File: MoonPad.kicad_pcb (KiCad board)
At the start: 4 copper layers, 44.5 x 40.6 mm, 61 parts, among them IC1 W25Q16JVUXIQ, J1 OLED, J3 USB-C 2.0 Receptacle, SW1 Reset, U3 RP2040, U4 SLSS49E-3, U5 SLSS49E-3, U6 AP2112K-3.3, Y1 JGHC S3212000181080

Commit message: Fixed libraries
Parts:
- D4: footprint kicad-keyboard-parts:MX_SK6812MINI-E_REV -> Moonpad:MX_SK6812MINI-E_REV
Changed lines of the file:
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@@
     )
   )
-  (footprint "kicad-keyboard-parts:MX_SK6812MINI-E_REV" (layer "F.Cu")
+  (footprint "Moonpad:MX_SK6812MINI-E_REV" (layer "F.Cu")
     (at 156.21 110.49)
     (descr "Add-on for regular MX-footprints with SK6812 MINI-E")
@@
     (fp_arc (start 1.046711 -1.592299) (mid 1.638072 -1.528035) (end 1.749484 -0.943719)
       (stroke (width 0.1) (type solid)) (layer "Edge.Cuts"))
-    (fp_arc (start 1.699999 -0.726842) (mid 1.712528 -0.838068) (end 1.749484 -0.94372)
+    (fp_arc (start 1.699999 -0.726842) (mid 1.712527 -0.838068) (end 1.749484 -0.94372)
       (stroke (width 0.1) (type solid)) (layer "Edge.Cuts"))
     (fp_arc (start 1.749484 0.89572) (mid 1.63807 1.480034) (end 1.046711 1.544298)
@@
       (rotate (xyz 0 0 0))
     )
-    (model "${KIPRJMOD}/Libraries/kicad-keyboard-parts.pretty/3d/LED_SK6812MINI-E.step"
+    (model "${KIPRJMOD}/Libraries/marbastlib/3dmodels/LED_SK6812MINI-E.step"
       (offset (xyz 0 -5.08 -1.778))
       (scale (xyz 1 1 1))
@@
     (fp_arc (start 1.046711 -1.592299) (mid 1.638072 -1.528035) (end 1.749484 -0.943719)
       (stroke (width 0.1) (type solid)) (layer "Edge.Cuts"))
-    (fp_arc (start 1.699999 -0.726842) (mid 1.712528 -0.838068) (end 1.749484 -0.94372)
+    (fp_arc (start 1.699999 -0.726842) (mid 1.712527 -0.838068) (end 1.749484 -0.94372)
       (stroke (width 0.1) (type solid)) (layer "Edge.Cuts"))
     (fp_arc (start 1.749484 0.89572) (mid 1.63807 1.480034) (end 1.046711 1.544298)
@@
       (rotate (xyz 0 0 0))
     )
-    (model "${KIPRJMOD}/Libraries/kicad-keyboard-parts.pretty/3d/LED_SK6812MINI-E.step"
+    (model "${KIPRJMOD}/Libraries/marbastlib/3dmodels/LED_SK6812MINI-E.step"
       (offset (xyz 0 -5.08 -1.778))
       (scale (xyz 1 1 1))

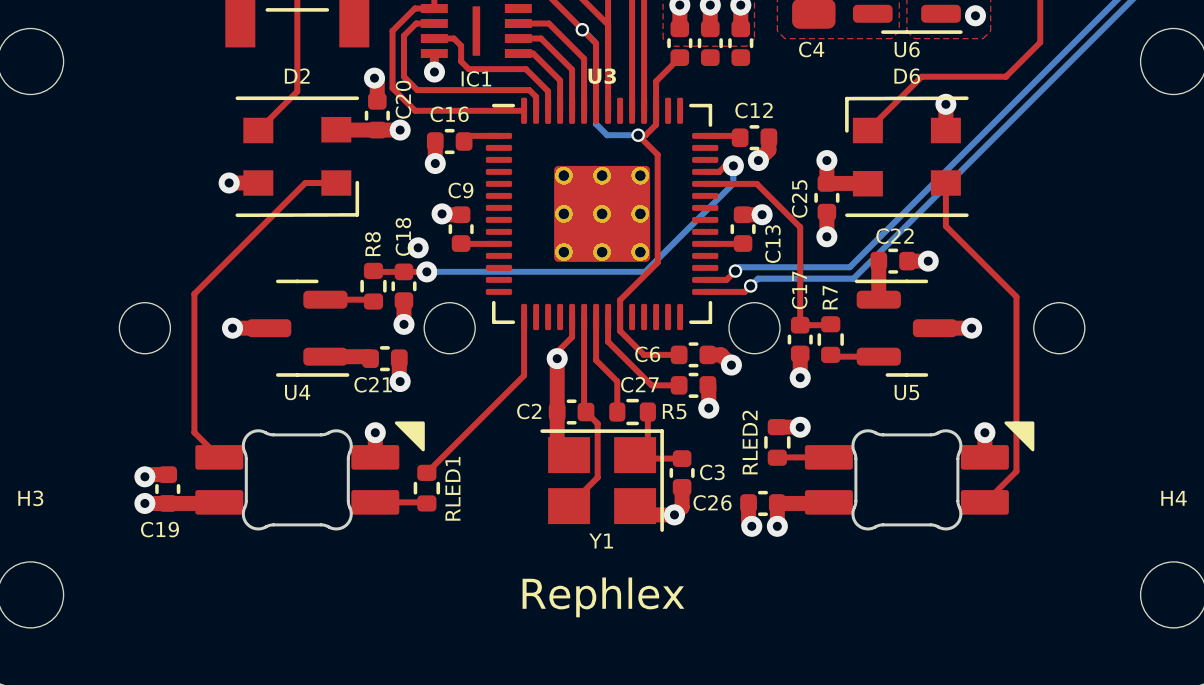
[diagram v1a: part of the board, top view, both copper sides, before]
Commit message: Edited some 3d. Now sent for manufacturing.
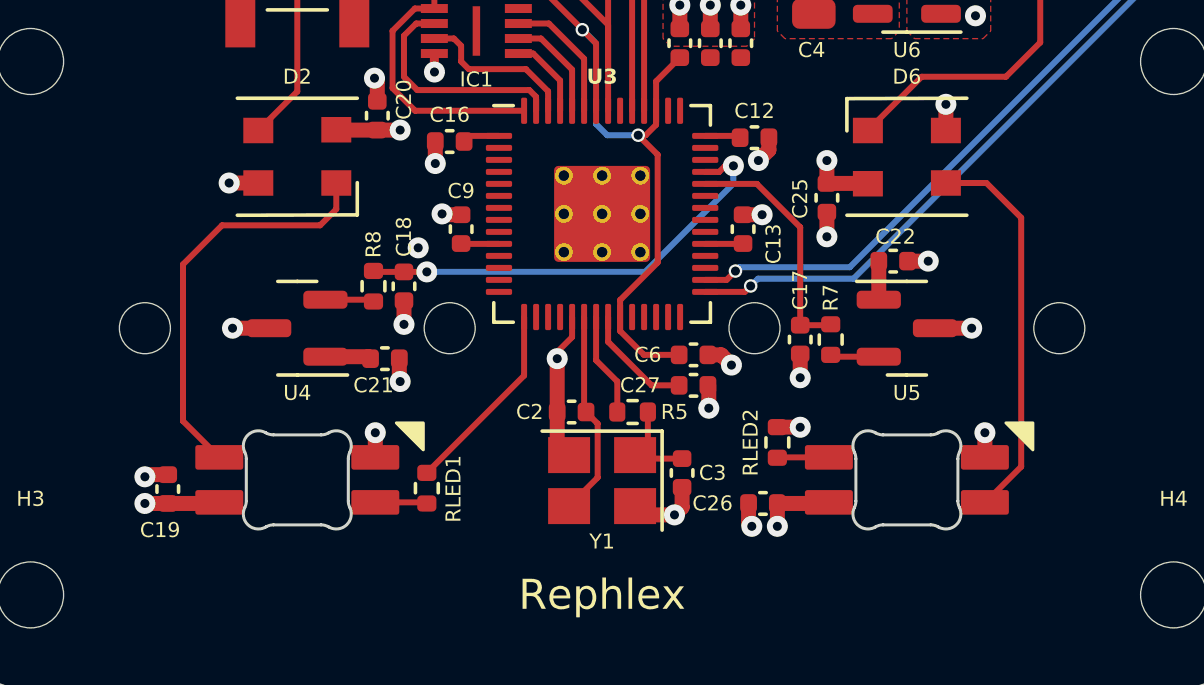
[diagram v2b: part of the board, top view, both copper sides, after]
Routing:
- net Net-(D1-DOUT): track 12.1 -> 13.7 mm
- net Net-(D4-DIN): track 12.1 -> 13.0 mm
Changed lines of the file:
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@@
       (net 2 "GND") (pinfunction "SHIELD") (pintype "passive"))
     (model "${KIPRJMOD}/Libraries/TYPE-C-31-M-12--3DModel-STEP-56544.STEP"
-      (offset (xyz 0 -1.143 0))
+      (offset (xyz 0 -1.05 0))
       (scale (xyz 1 1 1))
       (rotate (xyz 90 180 180))
@@
     (property "ki_description" "Resistor")
     (property "ki_keywords" "R res resistor")
-    (attr smd)
+    (attr smd exclude_from_pos_files exclude_from_bom)
     (fp_text reference "R9" (at 0 1.257236) (layer "F.SilkS") hide
         (effects (font (size 0.5 0.5) (thickness 0.125)))
@@
       (rotate (xyz 0 0 0))
     )
+    (model "${KIPRJMOD}/shapes3D/OLED-Module-with-Pins.wrl"
+      (offset (xyz 0 -3.81 0))
+      (scale (xyz 1 1 1))
+      (rotate (xyz 0 0 -90))
+    )
   )
   (gr_rect (start 125.73 95.25) (end 166.37 115.57)
@@
   (segment (start 135.89 97.52) (end 134.59 98.82) (width 0.2) (layer "F.Cu") (net 60))
   (segment (start 137.19 85.33) (end 135.89 86.63) (width 0.2) (layer "F.Cu") (net 60))
-  (segment (start 132.461 104.267) (end 132.461 108.887) (width 0.2) (layer "F.Cu") (net 61))
-  (segment (start 137.19 100.57) (end 136.158 100.57) (width 0.2) (layer "F.Cu") (net 61))
-  (segment (start 136.158 100.57) (end 132.461 104.267) (width 0.2) (layer "F.Cu") (net 61))
-  (segment (start 132.461 108.887) (end 133.29 109.716) (width 0.2) (layer "F.Cu") (net 61))
+  (segment (start 137.19 100.57) (end 137.19 101.443) (width 0.2) (layer "F.Cu") (net 61))
+  (segment (start 132.08 103.28275) (end 132.08 108.506) (width 0.2) (layer "F.Cu") (net 61))
+  (segment (start 137.19 101.443) (end 136.652 101.981) (width 0.2) (layer "F.Cu") (net 61))
+  (segment (start 133.38175 101.981) (end 132.08 103.28275) (width 0.2) (layer "F.Cu") (net 61))
+  (segment (start 132.08 108.506) (end 133.29 109.716) (width 0.2) (layer "F.Cu") (net 61))
+  (segment (start 136.652 101.981) (end 133.38175 101.981) (width 0.2) (layer "F.Cu") (net 61))
   (segment (start 138.49 111.216) (end 140.172 111.216) (width 0.2) (layer "F.Cu") (net 62))
   (segment (start 140.172 111.216) (end 140.208 111.252) (width 0.2) (layer "F.Cu") (net 62))
@@
   (segment (start 160.655 87.503) (end 158.482 85.33) (width 0.2) (layer "F.Cu") (net 63))
   (segment (start 160.655 95.885) (end 160.655 87.503) (width 0.2) (layer "F.Cu") (net 63))
-  (segment (start 157.51 102.011) (end 159.8624 104.3634) (width 0.2) (layer "F.Cu") (net 64))
-  (segment (start 159.8624 104.3634) (end 159.8624 110.182513) (width 0.2) (layer "F.Cu") (net 64))
-  (segment (start 159.8624 110.182513) (end 158.828913 111.216) (width 0.2) (layer "F.Cu") (net 64))
+  (segment (start 160.02 110.024913) (end 158.828913 111.216) (width 0.2) (layer "F.Cu") (net 64))
+  (segment (start 160.02 101.727) (end 160.02 110.024913) (width 0.2) (layer "F.Cu") (net 64))
   (segment (start 158.828913 111.216) (end 158.81 111.216) (width 0.2) (layer "F.Cu") (net 64))
-  (segment (start 157.51 100.57) (end 157.51 102.011) (width 0.2) (layer "F.Cu") (net 64))
+  (segment (start 157.51 100.57) (end 158.863 100.57) (width 0.2) (layer "F.Cu") (net 64))
+  (segment (start 158.863 100.57) (end 160.02 101.727) (width 0.2) (layer "F.Cu") (net 64))
   (segment (start 131.572 111.252) (end 133.254 111.252) (width 0.5) (layer "F.Cu") (net 65))
   (segment (start 138.557 83.566) (end 139.319 83.566) (width 0.5) (layer "F.Cu") (net 65))

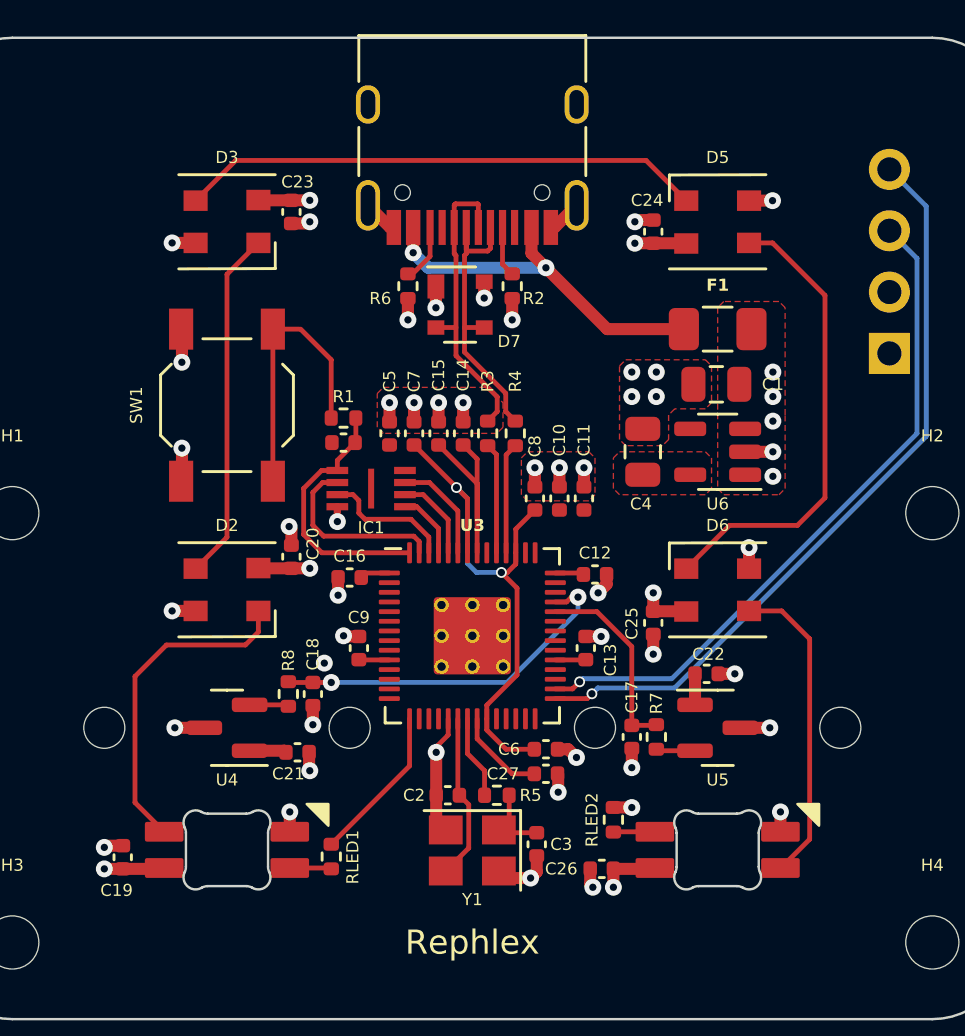
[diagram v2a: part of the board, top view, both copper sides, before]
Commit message: Cost optimisation + case files
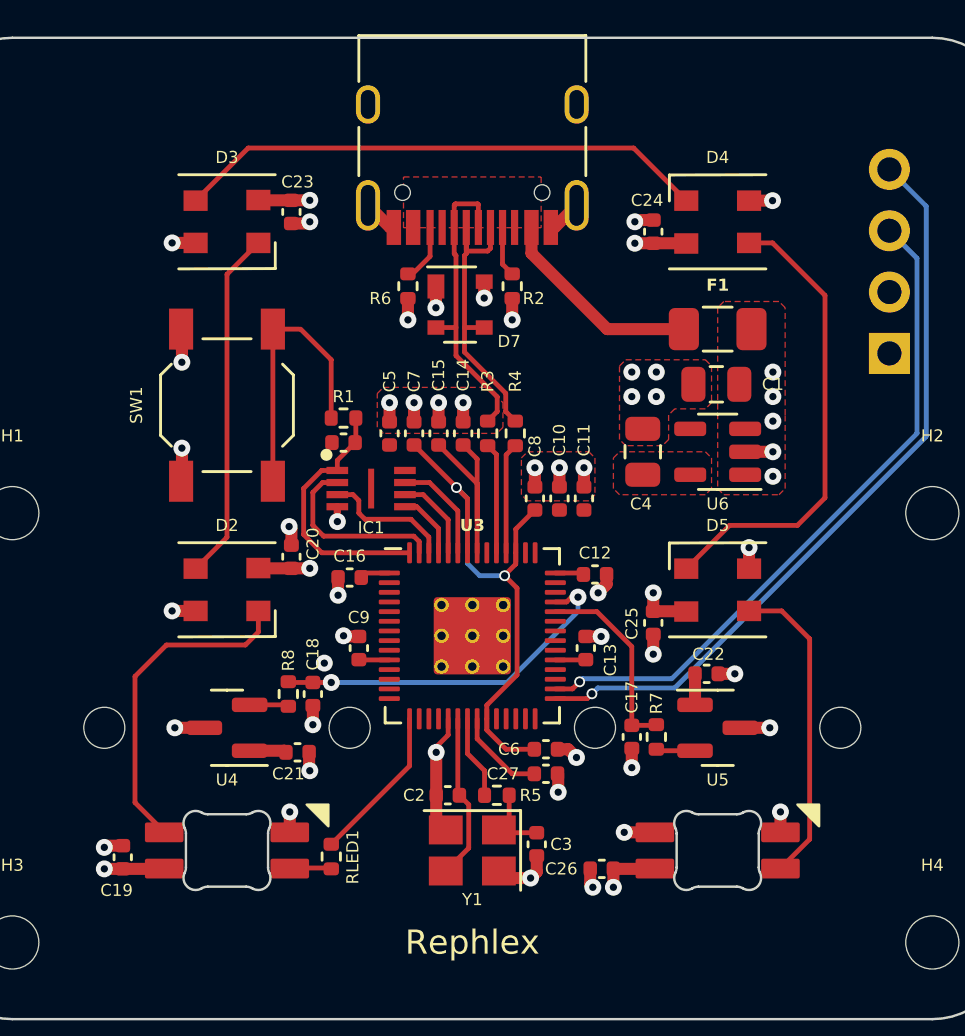
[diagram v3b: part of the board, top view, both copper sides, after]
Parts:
- removed RLED2: 470, Resistor_SMD:R_0402_1005Metric
- C2, C3: value 27p -> 30p
- D6: renamed from D4; footprint Moonpad:MX_SK6812MINI-E_REV -> kicad-keyboard-parts:MX_SK6812MINI-E_REV
- Y1: value JGHC S3212000181080 -> X322512MSB4SI
- moved D1 0.10 mm to (135.8, 110.5)
- moved D6 0.10 mm to (156.1, 110.5)
- renumbered D5 to D4, D6 to D5
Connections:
- D6 pad 2: Net-(D4-DOUT) (its old number) -> GND
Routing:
- net VBUS: track 15.5 -> 8.68 mm, vias 2 -> 0
- net Net-(D4-DOUT) (its old number): track 1.70 -> 0.00 mm
- net GND: track 44.1 -> 44.6 mm
- added copper zone on F.Cu, net VBUS
